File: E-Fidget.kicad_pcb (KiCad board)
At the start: 4 copper layers, 70 x 70 mm, 91 parts, among them J1 Conn_01x02, J2 USB_B_Micro, J3 Barrel_Jack_MountingPin, M1 Motor_DC, M2 Motor_DC, M3 Motor_DC, M4 Motor_DC, M5 Motor_DC, M6 Motor_DC, M7 Motor_DC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

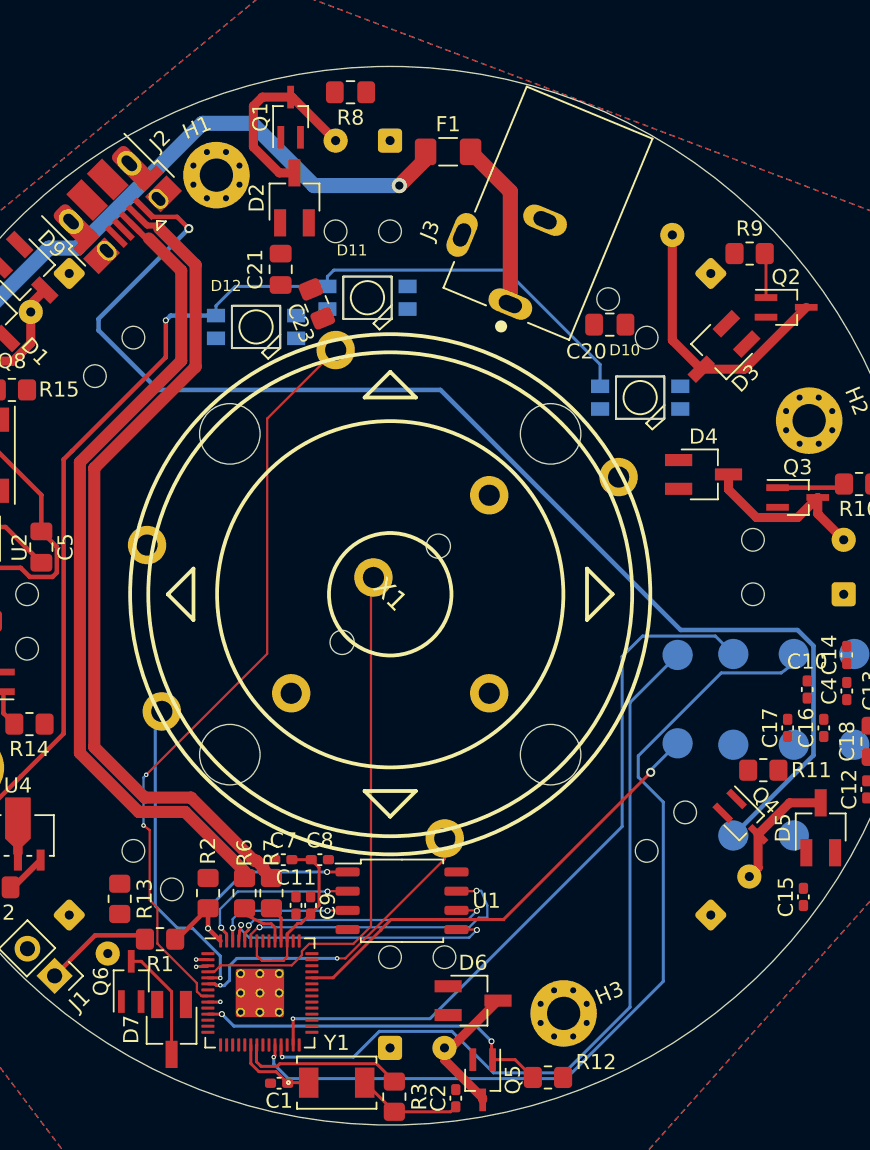
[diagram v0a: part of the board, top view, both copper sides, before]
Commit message: Route some traces (56 unrouted pads)
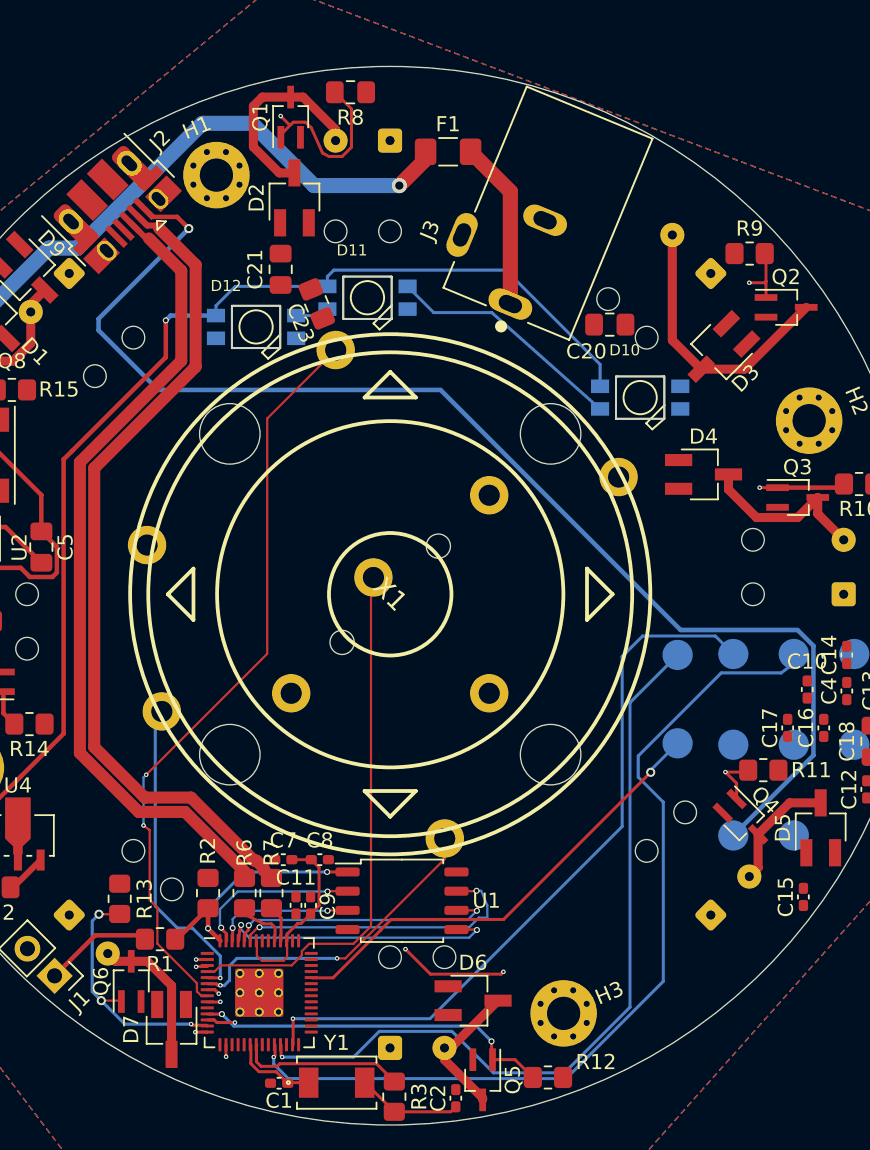
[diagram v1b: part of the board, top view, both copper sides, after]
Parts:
- added kibuzzard-62FBD247: G***, kibuzzard-62FBD247, B.Cu at (146.6, 98.6)
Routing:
- net /GPIO7: track 0.83 -> 79.2 mm, vias 1 -> 2
- net /GPIO11: track 2.94 -> 75.7 mm, vias 0 -> 2
- net /GPIO13: track 4.49 -> 64.9 mm, vias 0 -> 2
- net /GPIO5: track 0.00 -> 49.8 mm, vias 0 -> 1
- net /GPIO9: track 0.00 -> 48.1 mm, vias 0 -> 4
- net /GPIO10: track 0.00 -> 16.6 mm, vias 0 -> 3
- net Net-(D10-Pad2-DOUT): track 0.00 -> 15.9 mm
- net Net-(D11-Pad2-DOUT): track 0.00 -> 2.24 mm
- net Net-(D7-Pad2): track 7.65 -> 9.65 mm
- net /GPIO1: track 39.6 -> 39.1 mm

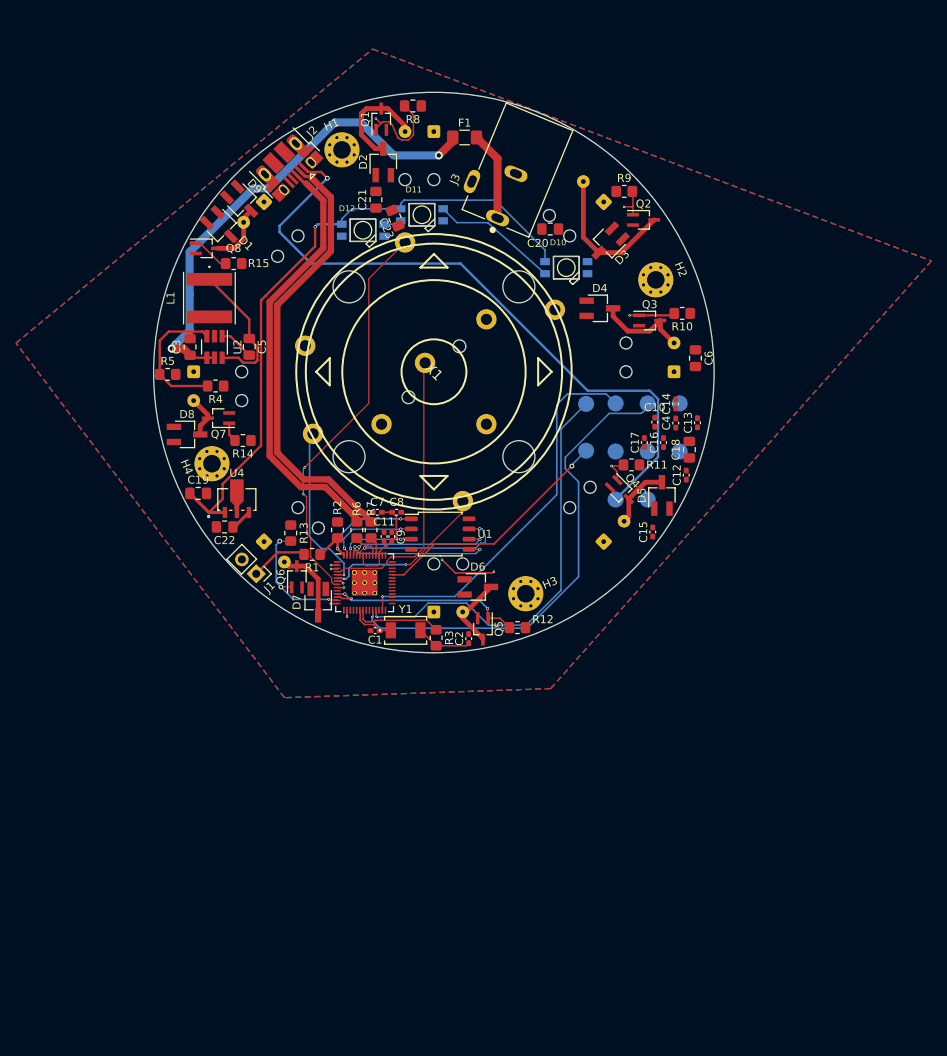
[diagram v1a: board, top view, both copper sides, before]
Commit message: Finish routing traces & fix DRC errors
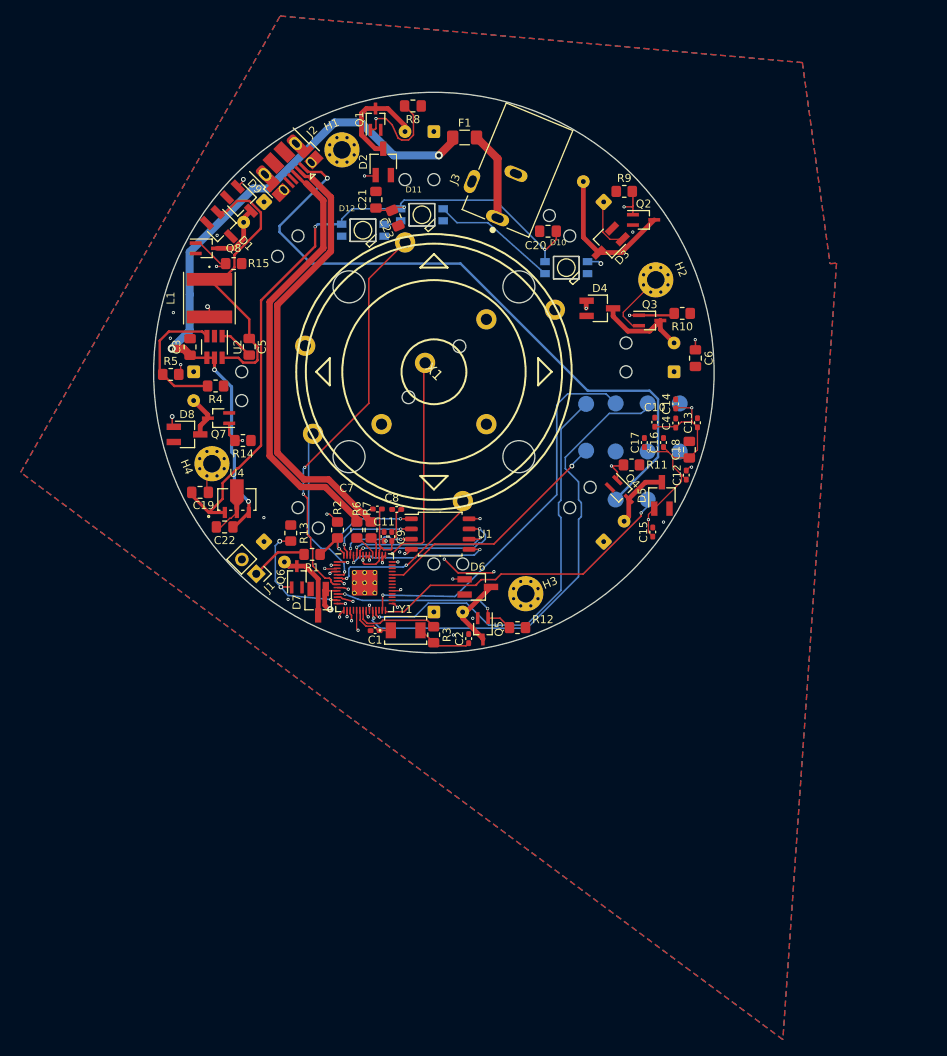
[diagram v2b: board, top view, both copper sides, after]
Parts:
- removed kibuzzard-62FBD247: G***, kibuzzard-62FBD247
- added kibuzzard-6302439D: G***, kibuzzard-6302439D, B.Cu at (145.1, 99.5)
- moved Q1 0.71 mm to (139.8, 73.4)
- moved R3 0.49 mm to (147.0, 137.8)
- moved C7 0.41 mm to (140.0, 122.1)
- moved C20 0.39 mm to (161.3, 87.4)
- moved R5 0.38 mm to (114.2, 105.3)
- moved C8 0.36 mm to (142.4, 122.1), turned to 180 degrees
- moved C19 0.26 mm to (117.8, 120.0)
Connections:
- TP4 pad 1: +3.3V -> +3V3
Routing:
- net +3V3: track 0.00 -> 66.3 mm, vias 0 -> 22
- net /GPIO18: track 0.00 -> 59.5 mm, vias 0 -> 2
- net /GPIO14: track 4.80 -> 60.2 mm, vias 0 -> 2
- net /GPIO17: track 0.00 -> 39.3 mm, vias 0 -> 1
- net /GPIO12: track 2.44 -> 32.2 mm, vias 0 -> 2
- net +9V: track 64.0 -> 85.1 mm, vias 2 -> 4
- net GND: track 0.00 -> 18.6 mm, vias 0 -> 13
- net Net-(C5-Pad2): track 17.4 -> 35.9 mm
- net +1V1: track 12.2 -> 23.3 mm, vias 0 -> 2
- net /GPIO2: track 35.3 -> 41.8 mm, vias 0 -> 2
- net +5V: track 81.4 -> 87.8 mm, vias 1 -> 3
- net /GPIO7: track 79.2 -> 81.2 mm
- net /GPIO11: track 75.7 -> 74.6 mm
- net /QSPI_SCLK: track 18.0 -> 18.5 mm

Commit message: Add some text to the bottom silkscreen
Added the revision (0.1b) and "JLCJLCJLCJLC" to tell JLCPCB where to place the order number.
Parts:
- added kibuzzard-6304F62D: G***, kibuzzard-6304F62D, B.Cu at (152.5, 106.7)
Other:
- board text added: "JLCJLCJLCJLC"
